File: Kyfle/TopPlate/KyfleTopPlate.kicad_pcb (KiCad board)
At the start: 2 copper layers, 160.8 x 138.4 mm, 44 parts, among them SW2 KEY_SWITCH, SW2 PRO MICRO

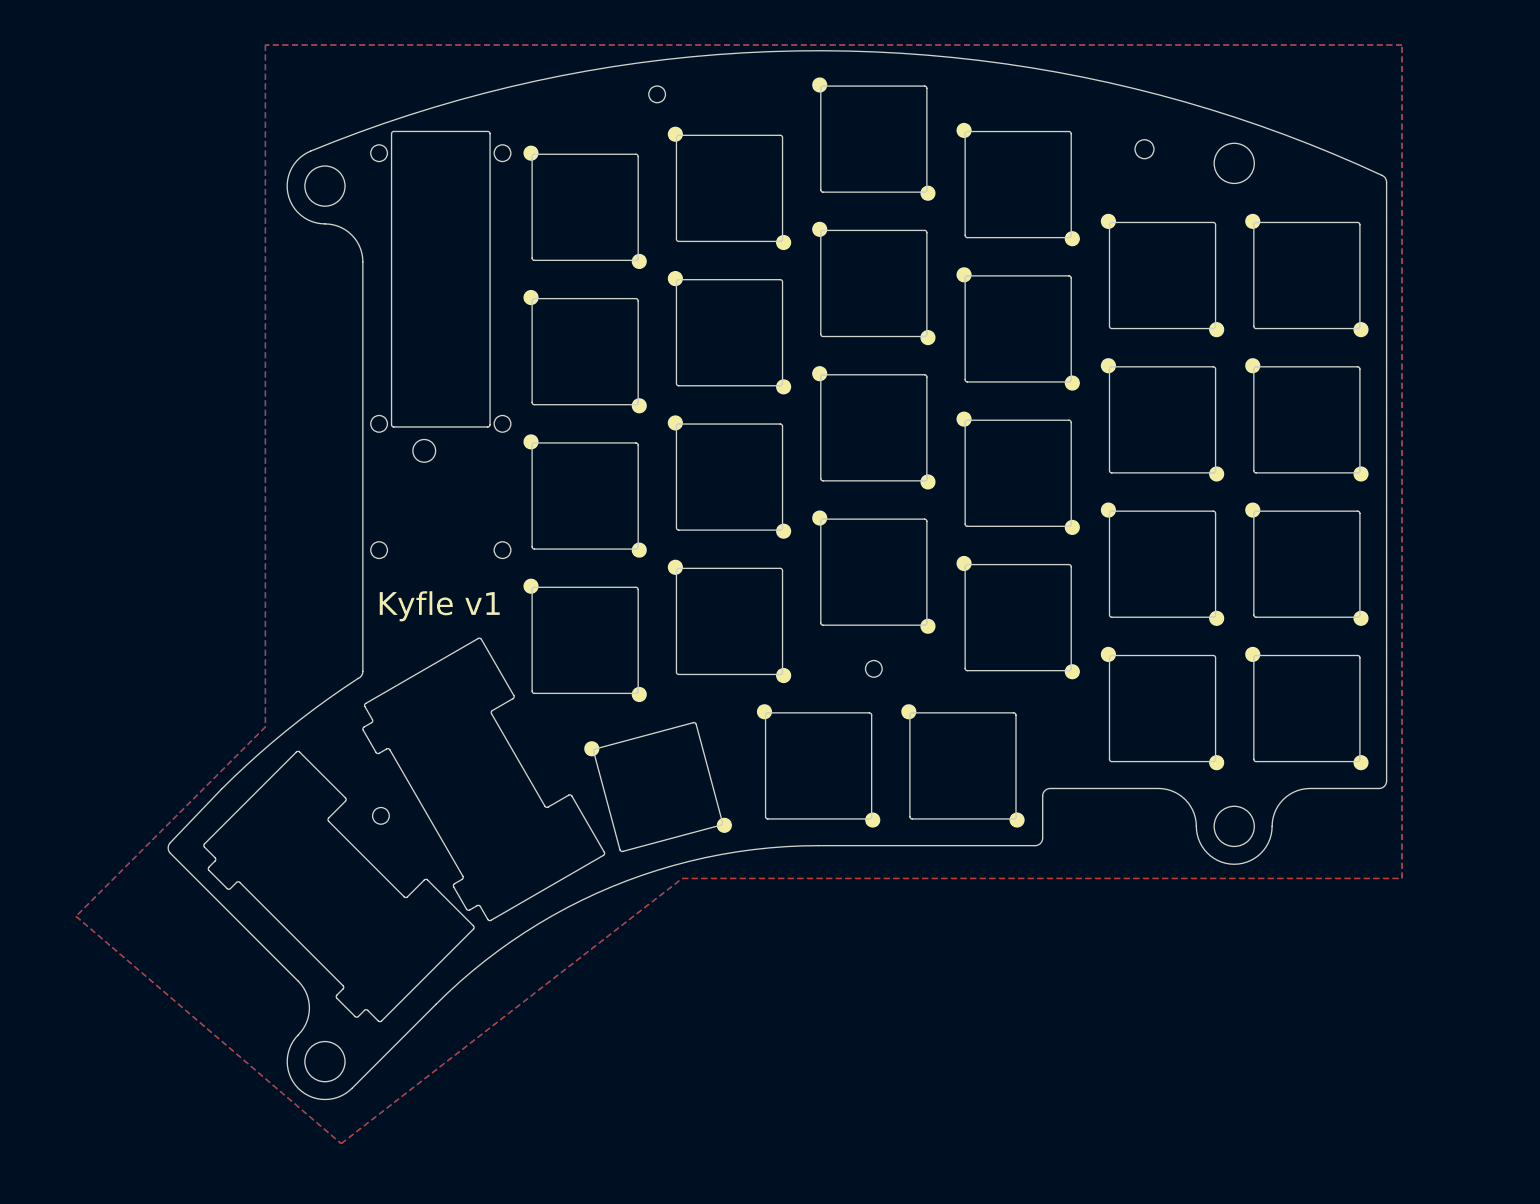
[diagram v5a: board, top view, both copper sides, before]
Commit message: Adding bottom plate
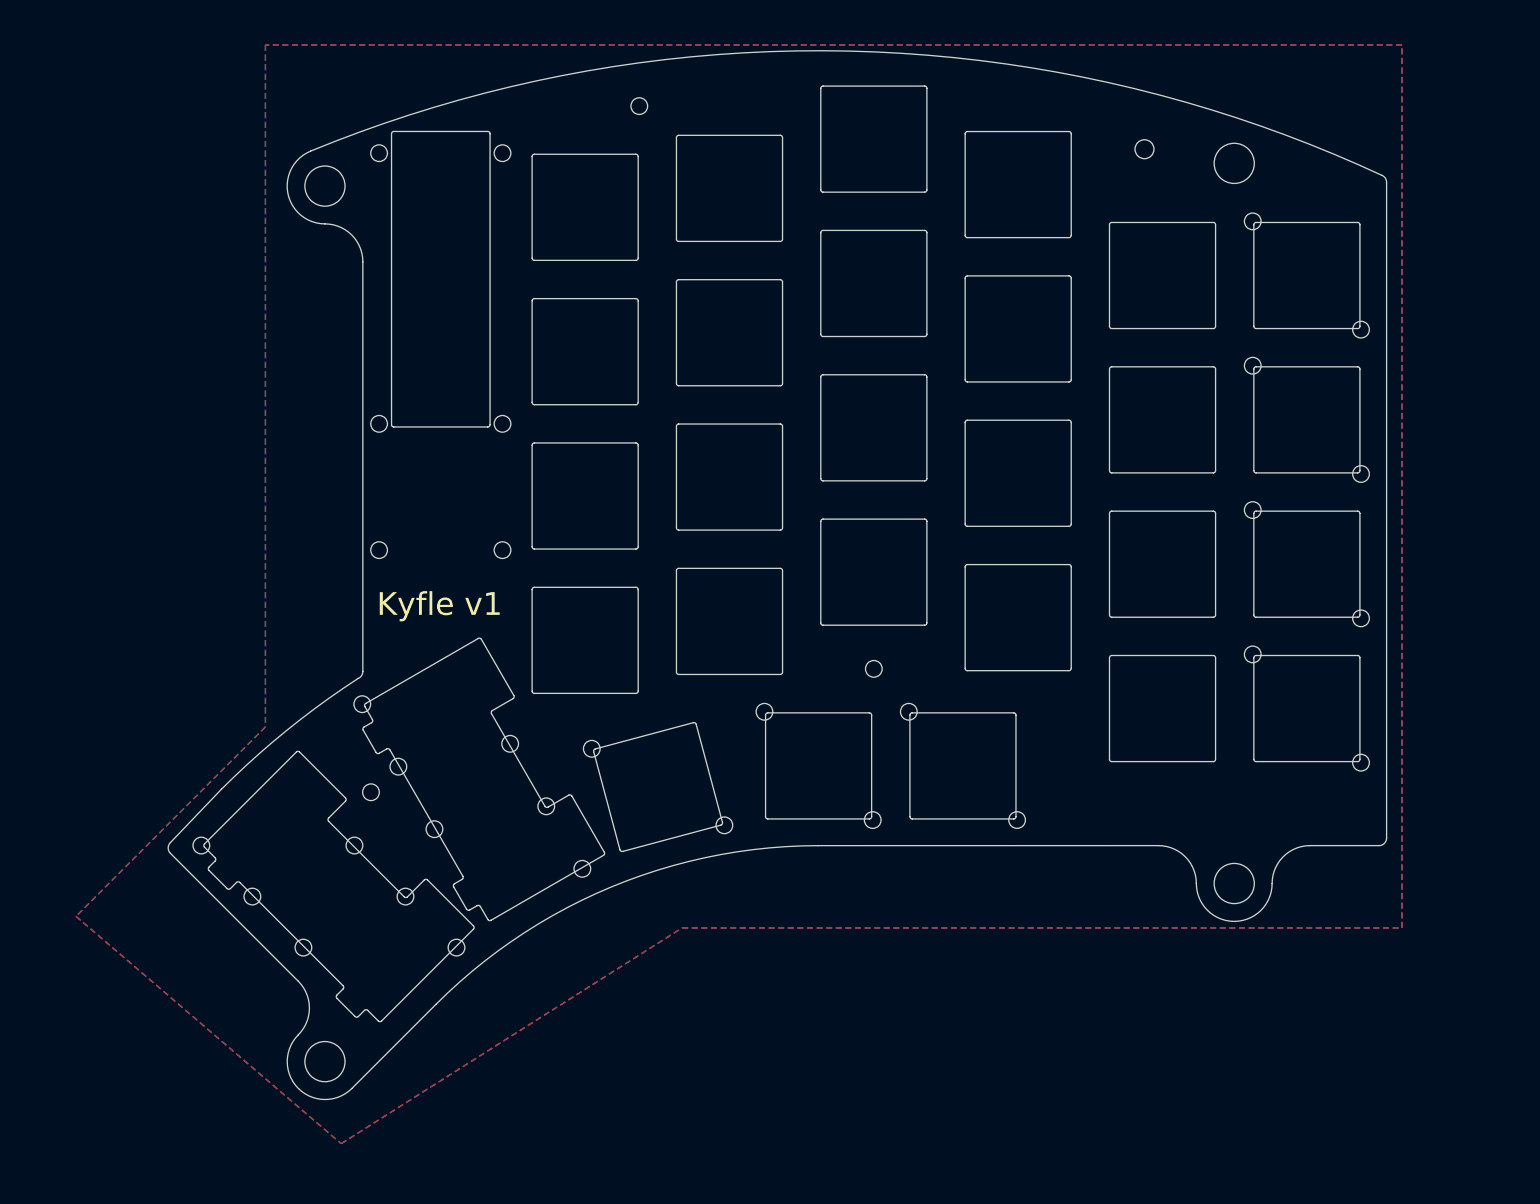
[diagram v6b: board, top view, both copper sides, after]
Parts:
- SW2 (x7): footprint SofleChocTop:SU120_RGB_SW_Top -> SofleChocTop:SU120_RGB_SW_Top_drilled
- moved REF** 7.54 mm to (216.6, 133.6)
- moved TH7 3.38 mm to (102.7, 121.6), turned to 180 degrees
- moved TH3 2.82 mm to (138.1, 31.0)
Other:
- outline, holes or cut-outs redrawn

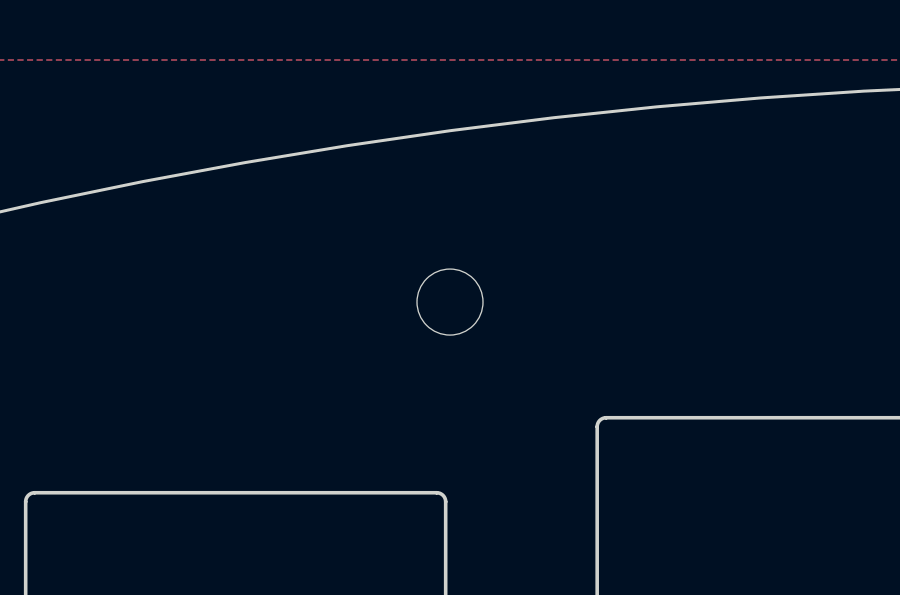
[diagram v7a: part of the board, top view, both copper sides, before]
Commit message: Adding reference positions to bottom plate silk screen
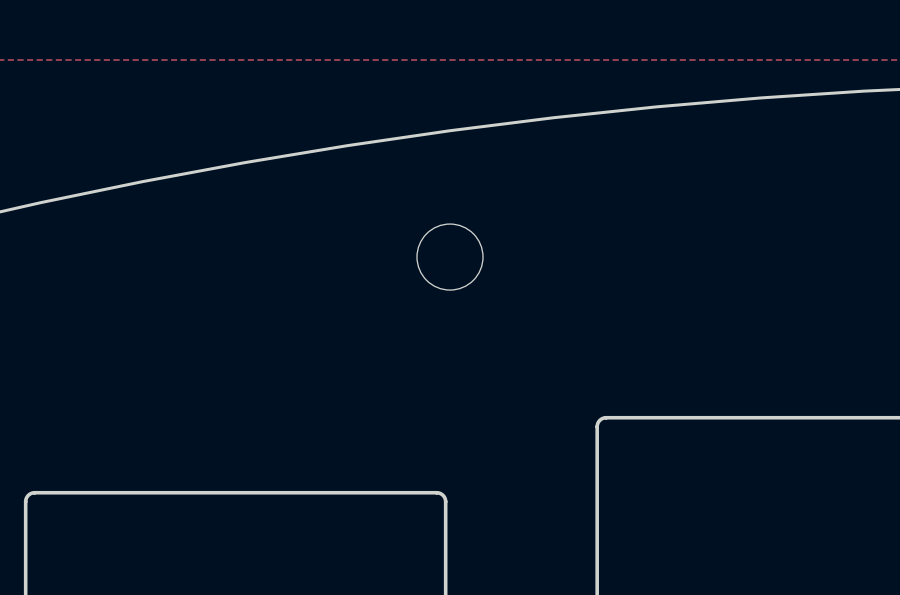
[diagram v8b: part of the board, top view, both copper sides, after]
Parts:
- moved TH3 1.50 mm to (138.1, 29.5)
